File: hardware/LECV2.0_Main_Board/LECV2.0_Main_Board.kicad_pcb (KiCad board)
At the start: 2 copper layers, 146 x 145.3 mm, 44 parts, among them J1 LED Indicator Connector, J10 Conn_01x02, J2 Ox Main, J3 Fuel Main, J4 Conn_02x07_Odd_Even, Q1 BUK6Y33-60PX, Q3 Q_NPN, U1 Pico, U2 INA_237, U3 LMR33640ADDAR, U4 W25Q128JVSIQ, U5 Adafruit LSM6DSOX + LIS3MDL, U6 XBee_HAT

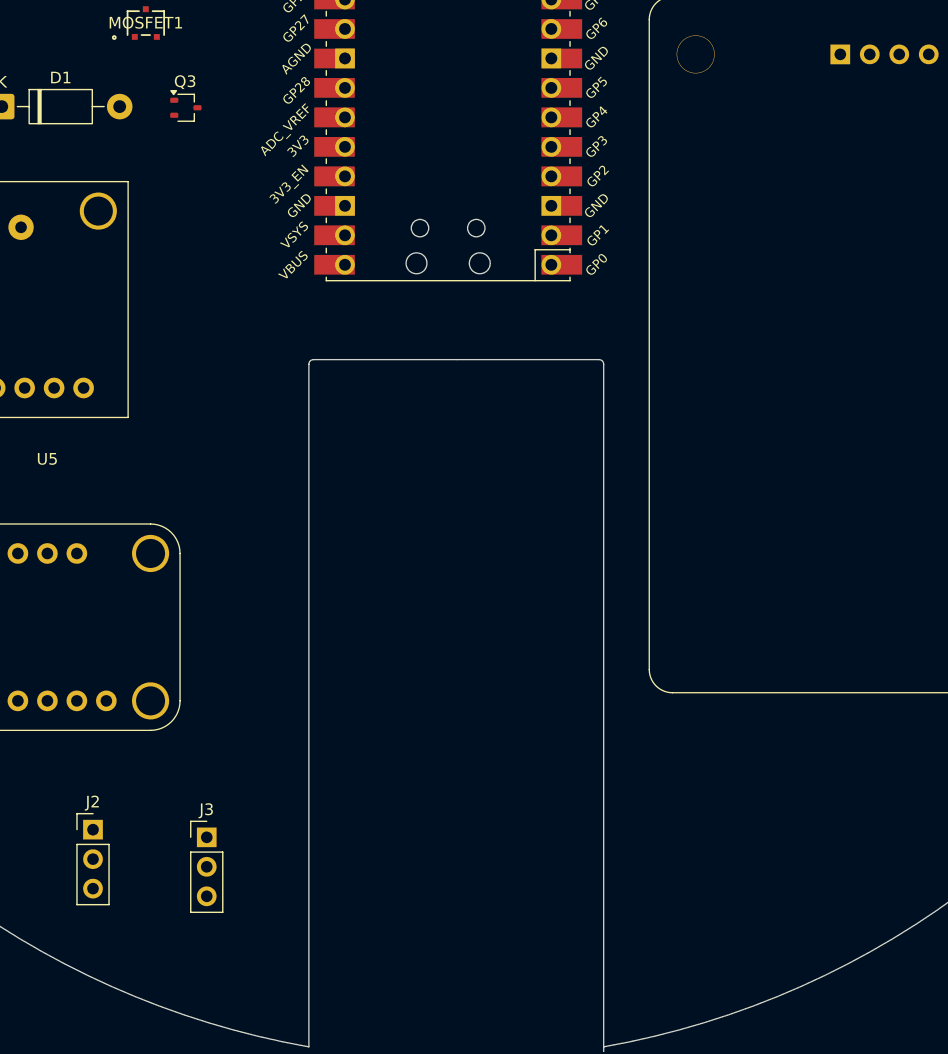
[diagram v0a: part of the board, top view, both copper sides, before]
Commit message: Fixed all footprints. Defined PCB edge, arbitrarily placed components
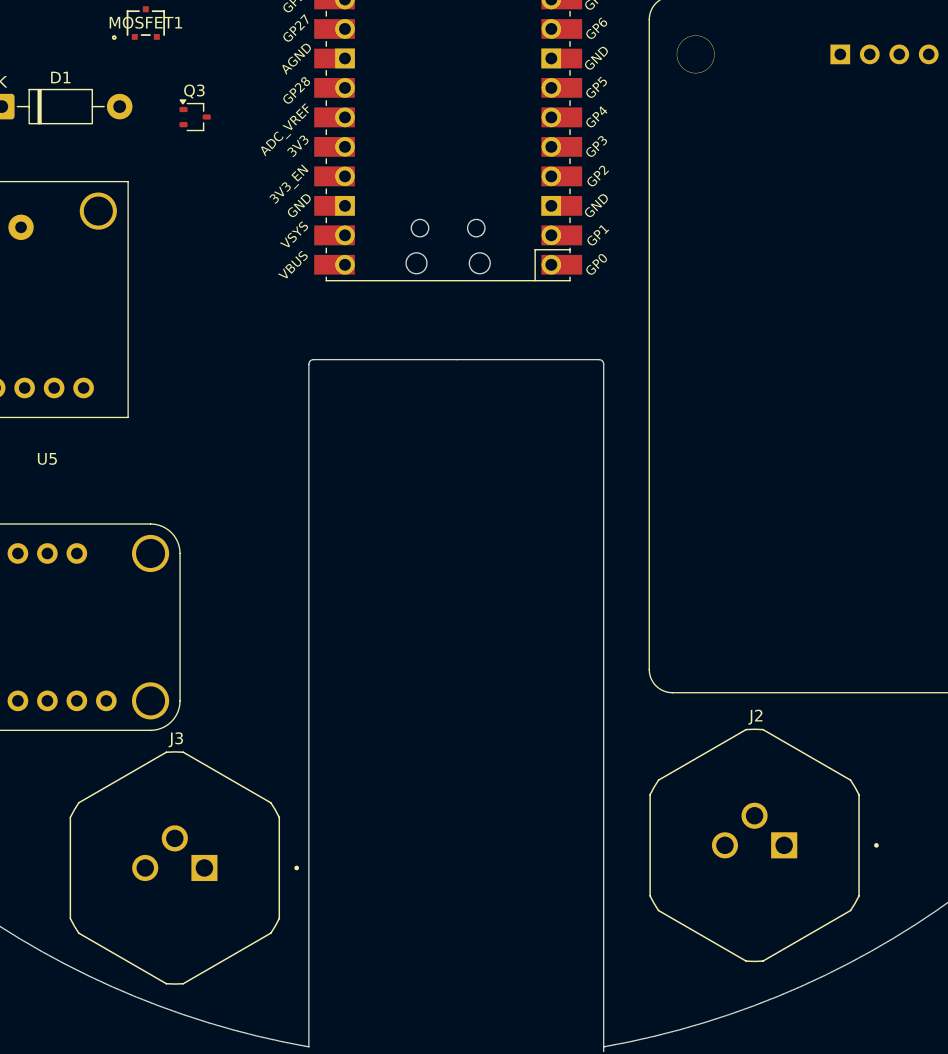
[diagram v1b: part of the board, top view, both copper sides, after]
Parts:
- J2, J3: footprint Connector_PinHeader_2.54mm:PinHeader_1x03_P2.54mm_Vertical -> 54-00440:TENSILITY_54-00440
- moved J2 57.0 mm to (176.9, 144.8)
- moved J3 3.81 mm to (127.0, 146.7)
- moved Q3 1.13 mm to (128.7, 82.0)

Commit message: Added GPIO clamping diodes, sufficient buck output capacitance, UVLO divider, and 3V3_EN diode
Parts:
- added C13: 22 uF, Capacitor_SMD:C_0805_2012Metric, F.Cu at (84.6, 36.0)
- added C14: 22 uF, Capacitor_SMD:C_0805_2012Metric, F.Cu at (84.6, 39.0)
- added C15: 22 uF, Capacitor_SMD:C_0805_2012Metric, F.Cu at (84.6, 42.1)
- added D2: 1N5817, Diode_THT:D_DO-41_SOD81_P10.16mm_Horizontal, F.Cu at (68.4, 36.7)
- added R10: 2.49k, Resistor_SMD:R_0603_1608Metric, F.Cu at (88.9, 35.8)
- added R11: 10K, Resistor_SMD:R_0603_1608Metric, F.Cu at (88.9, 38.3)
- added R12: 1k, Resistor_SMD:R_0603_1608Metric, F.Cu at (73.7, 40.0)
- added R13: 1k, Resistor_SMD:R_0603_1608Metric, F.Cu at (73.7, 42.5)
- added U7: BAV199_215, Package_TO_SOT_SMD:SOT-23-3, F.Cu at (69.1, 41.2)
- added U8: BAV199_215, Package_TO_SOT_SMD:SOT-23-3, F.Cu at (69.1, 45.8)
- added U9: BAV199_215, Package_TO_SOT_SMD:SOT-23-3, F.Cu at (69.1, 50.4)
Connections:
- R1 pad 1: Net-(J3-Pin_3) -> Net-(U1-GPIO21)
- R3 pad 1: Net-(J2-Pin_3) -> Net-(U1-GPIO22)
- U1 pad 27: Net-(J3-Pin_3) -> Net-(U1-GPIO21)
- U1 pad 29: Net-(J2-Pin_3) -> Net-(U1-GPIO22)
- U1 pad 37: unconnected-(U1-3V3_EN-Pad37) -> Net-(D2-A)
- U3 pad 3: 11.1V -> Net-(U3-EN)

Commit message: Finished PCBs
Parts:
- removed C22, C24: 10u, Capacitor_SMD:C_0805_2012Metric
- removed D1, D2: 1N5817, Diode_THT:D_DO-41_SOD81_P10.16mm_Horizontal
- removed the REF** at (152.1, 23.5)
- removed the REF** at (217.1, 89.6)
- removed the REF** at (86.5, 90.5)
- removed U9: BAV199_215, Package_TO_SOT_SMD:SOT-23-3
- added ?: , , F.Cu at (145.5, 37.0)
- added ?: , , F.Cu at (156.9, 84.0)
- added ?: , , F.Cu at (156.9, 37.0)
- added C16: 10u, Capacitor_SMD:C_1210_3225Metric, F.Cu at (117.6, 124.4)
- added C17: 10u, Capacitor_SMD:C_1210_3225Metric, F.Cu at (94.6, 106.0)
- added C19: 10u, Capacitor_SMD:C_1210_3225Metric, F.Cu at (108.8, 35.4)
- added D3: D_Dual_Series_AKC_Parallel, Package_TO_SOT_SMD:SOT-23, F.Cu at (130.1, 78.7)
- added G***: LOGO, RDT_Logo:RDT_Logo, F.Cu at (201.3, 47.1)
- added REF**: MountingHole_5.3mm_M5, MountingHole:MountingHole_5.3mm_M5, F.Cu at (151.2, 25.7)
- added REF**: MountingHole_2.2mm_M2, MountingHole:MountingHole_2.2mm_M2, F.Cu at (128.2, 107.1)
- added REF**: MountingHole_2.2mm_M2, MountingHole:MountingHole_2.2mm_M2, F.Cu at (132.2, 154.7)
- added REF**: MountingHole_2.2mm_M2, MountingHole:MountingHole_2.2mm_M2, F.Cu at (183.4, 30.0)
- added REF**: MountingHole_2.2mm_M2, MountingHole:MountingHole_2.2mm_M2, F.Cu at (95.5, 50.7)
- added REF**: MountingHole_5.3mm_M5, MountingHole:MountingHole_5.3mm_M5, F.Cu at (215.7, 90.2)
- added REF**: MountingHole_2.2mm_M2, MountingHole:MountingHole_2.2mm_M2, F.Cu at (87.2, 111.5)
- added REF**: MountingHole_5.3mm_M5, MountingHole:MountingHole_5.3mm_M5, F.Cu at (86.7, 90.2)
- added REF**: MountingHole_2.2mm_M2, MountingHole:MountingHole_2.2mm_M2, F.Cu at (169.1, 154.9)
- C1, C18: footprint Capacitor_SMD:C_0805_2012Metric -> Capacitor_SMD:C_1210_3225Metric
- moved C12 87.0 mm to (106.2, 54.8), turned to 180 degrees
- moved R13 86.0 mm to (156.1, 67.0), turned to -90 degrees
- moved U7 83.0 mm to (148.5, 65.4), turned to 90 degrees
- moved R12 82.9 mm to (150.6, 70.9), turned to -90 degrees
- moved R6 81.9 mm to (106.3, 51.2), turned to 180 degrees
- moved U8 80.4 mm to (148.6, 58.0), turned to -90 degrees
- moved R8 78.7 mm to (109.6, 50.4)
- moved J2 78.4 mm to (104.2, 115.5), turned to 90 degrees
- moved U5 75.6 mm to (179.9, 152.3), turned to 180 degrees
- moved C10 68.8 mm to (111.5, 56.0)
- moved C8 66.9 mm to (119.7, 30.2), turned to 180 degrees
- moved L1 66.9 mm to (122.7, 48.5), turned to 90 degrees
- moved C4 65.8 mm to (115.5, 55.0), turned to 0 degrees
- moved C7 63.1 mm to (119.7, 33.8), turned to 180 degrees
- moved R9 59.8 mm to (122.4, 98.8), turned to -90 degrees
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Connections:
- net Net-(C9-Pad2) renamed Vin+ (INA237)
- net Net-(J10-Pin_2) renamed +BATT
- net Net-(U3-SW) renamed /Buck_Converter/SW
- C18 pad 1: Net-(J2-Pin_1) -> Net-(D3-K)
- J2 pad 1: Net-(J2-Pin_1) -> SrvoPwr (11.1V)
- J3 pad 1: Net-(J2-Pin_1) -> SrvoPwr (11.1V)
- J4 pad 1: +5V -> 11.1V
- J4 pad 10: /GPIO12 (CS (N2O) -> /GPIO12 (CS N2O)
- J4 pad 2: 11.1V -> +5V
- J4 pad 3: 11.1V -> /GPIO14 (FanCtrl)
- Q1 pad 5: Net-(J2-Pin_1) -> SrvoPwr (11.1V)
- R1 pad 1: Net-(U1-GPIO21) -> Net-(U1-GPIO26_ADC0)
- R12 pad 1: Net-(U1-GPIO22) -> Net-(U1-GPIO27_ADC1)
- R13 pad 1: Net-(U1-GPIO21) -> Net-(U1-GPIO26_ADC0)
- R3 pad 1: Net-(U1-GPIO22) -> Net-(U1-GPIO27_ADC1)
- R4 pad 1: /GPIO20 (LED_FET) -> /GPIO22 (LED_FET)
- R7 pad 2: /GPIO0 (Servo_PWR_Switch) -> /GPIO28 (Servo_PWR_Switch)
- U1 pad 1: /GPIO0 (UART_TX) -> /GPIO0 (Pico_TX)
- U1 pad 16: /GPIO12 (CS (N2O)) -> /GPIO12 (CS N2O)
- U1 pad 19: /GPIO14_(SDA_INA237) -> /GPIO14 (FanCtrl)
- U1 pad 2: /GPIO1 (UART_RX) -> /GPIO1 (Pico_RX)
- U1 pad 20: /GPIO15_(SCL_INA237) -> unconnected-(U1-GPIO15-Pad20)
- U1 pad 26: /GPIO20 (LED_FET) -> /GPIO20_(SDA_INA237)
- U1 pad 27: Net-(U1-GPIO21) -> /GPIO21_(SCL_INA237)
- U1 pad 29: Net-(U1-GPIO22) -> /GPIO22 (LED_FET)
- U1 pad 31: /GPIO26 (IMU_SDA) -> Net-(U1-GPIO26_ADC0)
- U1 pad 32: /GPIO27 (IMU_SCL) -> Net-(U1-GPIO27_ADC1)
- U1 pad 34: unconnected-(U1-GPIO28_ADC2-Pad34) -> /GPIO28 (Servo_PWR_Switch)
- U1 pad 39: Net-(D1-K) -> Net-(D3-K)
- U1 pad 4: /GPIO0 (Servo_PWR_Switch) -> /GPIO2 (IMU_SDA)
- U1 pad 5: unconnected-(U1-GPIO3-Pad5) -> /GPIO3 (IMU_SCL)
- U2 pad 8: /GPIO14_(SDA_INA237) -> /GPIO20_(SDA_INA237)
- U2 pad 9: /GPIO15_(SCL_INA237) -> /GPIO21_(SCL_INA237)
- U5 pad 4: /GPIO27 (IMU_SCL) -> /GPIO3 (IMU_SCL)
- U5 pad 5: /GPIO26 (IMU_SDA) -> /GPIO2 (IMU_SDA)
- U6 pad 1: +5V -> GND
- U6 pad 2: /GPIO0 (UART_TX) -> /GPIO1 (Pico_RX)
- U6 pad 3: /GPIO1 (UART_RX) -> /GPIO0 (Pico_TX)
- U6 pad 4: GND -> +5V
- U7 pad 3: Net-(U1-GPIO22) -> Net-(U1-GPIO27_ADC1)
- U8 pad 3: Net-(U1-GPIO21) -> Net-(U1-GPIO26_ADC0)
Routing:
- net +3.3V: track 0.00 -> 164.8 mm, vias 0 -> 9
- net +5V: track 0.00 -> 120.4 mm
- net 11.1V: track 0.00 -> 103.2 mm, vias 0 -> 2
- net Net-(J3-Pin_3): track 0.00 -> 95.1 mm
- net Net-(J2-Pin_3): track 0.00 -> 86.0 mm, vias 0 -> 2
- net /GPIO3 (IMU_SCL): track 0.00 -> 68.1 mm, vias 0 -> 2
- net /GPIO2 (IMU_SDA): track 0.00 -> 64.1 mm, vias 0 -> 2
- net /GPIO4 (MISO_ADC): track 0.00 -> 49.8 mm, vias 0 -> 2
- net /GPIO22 (LED_FET): track 0.00 -> 46.0 mm, vias 0 -> 4
- net /GPIO5 (CS_ADC): track 0.00 -> 40.4 mm, vias 0 -> 2
- net /GPIO21_(SCL_INA237): track 0.00 -> 40.2 mm, vias 0 -> 2
- net /GPIO6 (SCK_ADC): track 0.00 -> 39.6 mm, vias 0 -> 2
- net /GPIO20_(SDA_INA237): track 0.00 -> 38.2 mm, vias 0 -> 2
- net /GPIO7 (MOSI_ADC): track 0.00 -> 35.0 mm, vias 0 -> 2
- net /GPIO9 (CS Chamber Shell_1): track 0.00 -> 29.4 mm, vias 0 -> 2
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- added copper zone on F.Cu, net +5V
- added copper zone on F.Cu, net +BATT
- added copper zone on F.Cu, net /Buck_Converter/SW
- added copper zone on F.Cu, net 11.1V
- added copper zone on B.Cu, net GND
- added copper zone on F.Cu, net GND
- added copper zone on F.Cu, net SrvoPwr (11.1V)
- added copper zone on F.Cu, net Vin+ (INA237)
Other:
- board size 146 x 145.3 mm -> 146 x 144.9 mm
- board text added: "+"
- board text added: "+5V"
- board text added: "+VBat"
- board text added: "-"
- board text added: "11.1V"
- board text added: "3.3V"
- board text added: "3.3V in"
- board text added: "5V"
- board text added: "Board: LEC V2.0 Designed: 1/2026 Designer: Rakshak Sudhakaran"
- board text added: "CS ADC"
- board text added: "CS CSTC1"
- board text added: "CS CSTC2"
- board text added: "CS N2OTC"
- board text added: "DAQ HAT"
- board text added: "FanCtrl"
- board text added: "Flash IC"
- board text added: "Fuel Main"
- board text added: "GND"
- board text added: "H"
- board text added: "IMU"
- board text added: "INA237"
- board text added: "In"
- board text added: "Indicator LED"
- board text added: "L"
- board text added: "MISO ADC"
- board text added: "MISO TCIC"
- board text added: "MOSI ADC"
- board text added: "Out"
- board text added: "Ox Main"
- board text added: "PWM"
- board text added: "PWR Input"
- board text added: "SCK ADC"
- board text added: "SCK TCIC"
- board text added: "SCL"
- board text added: "SDA"
- board text added: "SW"
- board text added: "XBee HAT"
- board text added: "XBee Rx"
- board text added: "XBee Tx"
- board text added: "{ "ViaStitching": "0.2", "stitch_zone_0": { "HSpacing": "2", "VSpacing": "2", "HOffset": "0", "VOffset": "0", "Clearance": "0", "Randomize": false } }"
- board text added: "{ "ViaStitching": "0.2", "stitch_zone_0": { "HSpacing": "3", "VSpacing": "3", "HOffset": "0", "VOffset": "0", "Clearance": "2", "Randomize": false } }"
- board text added: "{ "ViaStitching": "0.2", "stitch_zone_0": { "HSpacing": "3", "VSpacing": "3", "HOffset": "0", "VOffset": "0", "Clearance": "5", "Randomize": false } }"
- board text added: "{ "ViaStitching": "0.2", "stitch_zone_0": { "HSpacing": "3.5", "VSpacing": "3.5", "HOffset": "0", "VOffset": "0", "Clearance": "2", "Randomize": false } }"
- board text added: "{ "ViaStitching": "0.2", "stitch_zone_0": { "HSpacing": "4", "VSpacing": "4", "HOffset": "0", "VOffset": "0", "Clearance": "2", "Randomize": false } }"
